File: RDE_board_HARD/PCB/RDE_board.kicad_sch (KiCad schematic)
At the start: 18 parts, among them J4 7772, J5 7772, J6 7772, J7 7772

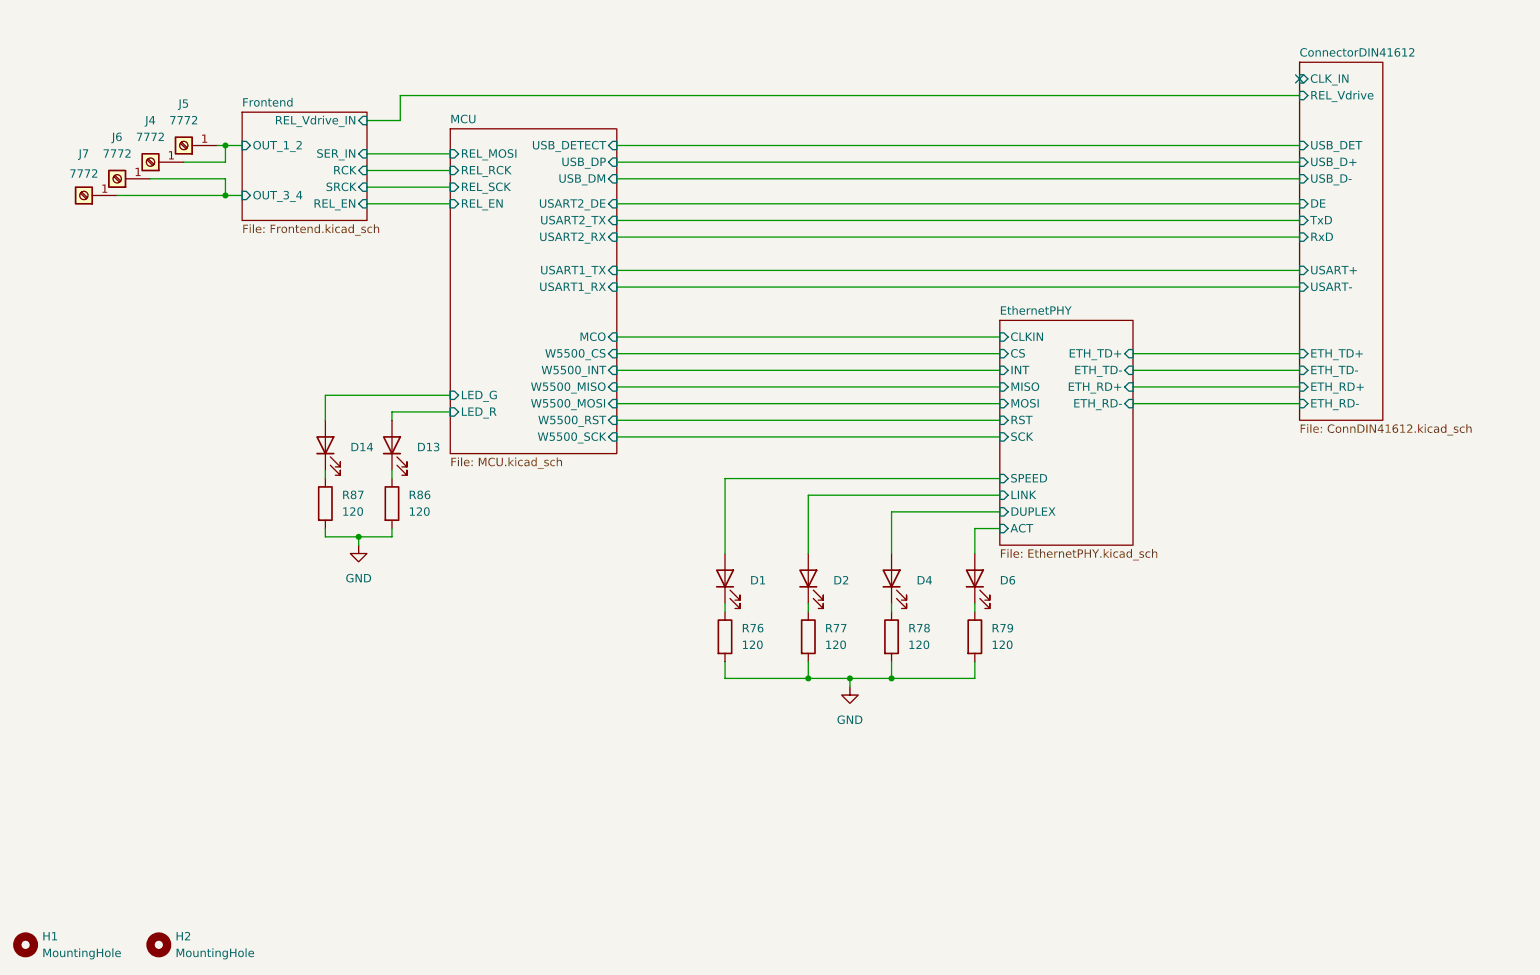
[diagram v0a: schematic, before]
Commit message: Added i2c for backplane config, testpoints. File organization
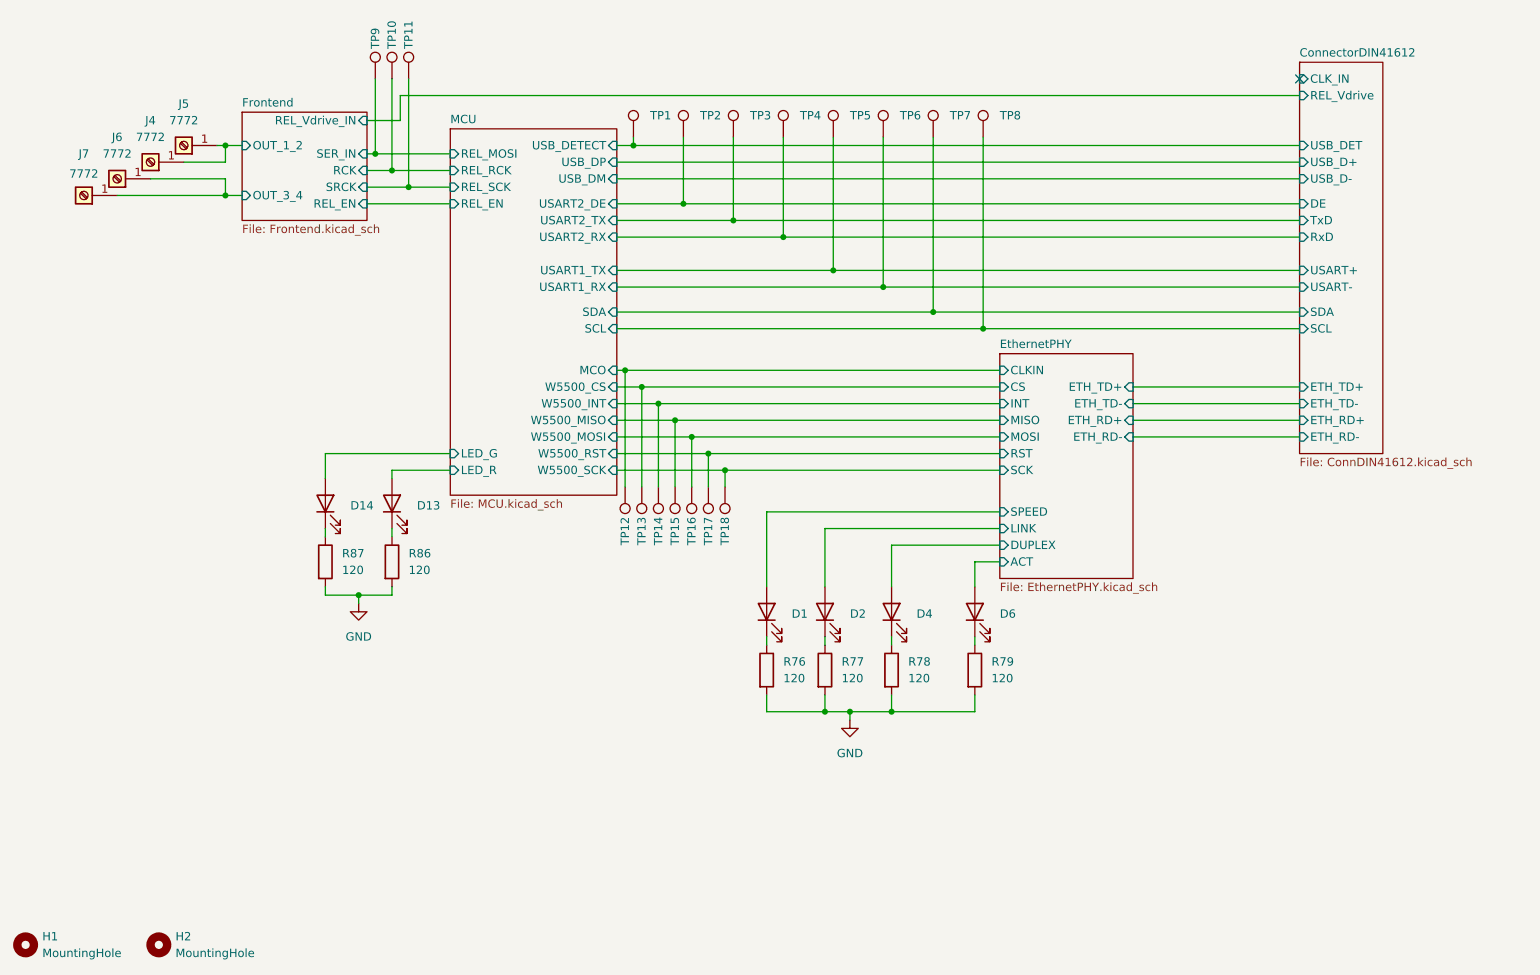
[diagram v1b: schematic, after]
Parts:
- added TP1, TP10, TP11, TP12, TP13, TP14, TP15, TP16, TP17, TP18, TP2, TP3, TP4, TP5, TP6, TP7, TP8, TP9: TestPoint, TestPoint:TestPoint_Pad_D1.0mm, symbol Connector:TestPoint
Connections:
- net ConnectorDIN41612/DE: now also TP2.1
- net ConnectorDIN41612/RxD: now also TP4.1
- net ConnectorDIN41612/TxD: now also TP3.1
- net ConnectorDIN41612/USART+: now also TP5.1
- net ConnectorDIN41612/USART-: now also TP6.1
- net ConnectorDIN41612/USB_DET: now also TP1.1
- net EthernetPHY/CLKIN: now also TP12.1
- net EthernetPHY/CS: now also TP13.1
- net EthernetPHY/INT: now also TP14.1
- net EthernetPHY/MISO: now also TP15.1
- net EthernetPHY/MOSI: now also TP16.1
- net EthernetPHY/RST: now also TP17.1
- net EthernetPHY/SCK: now also TP18.1
- net Frontend/RCK: now also TP10.1
- net Frontend/SER_IN: now also TP9.1
- net Frontend/SRCK: now also TP11.1
- new net ConnectorDIN41612/SCL: TP8.1
- new net ConnectorDIN41612/SDA: TP7.1
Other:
- sheet ConnectorDIN41612 ports: added SCL, SDA; removed none
- sheet MCU ports: added SCL, SDA; removed none
- moved on the sheet: D1, D13, D14, D2, D4, D6, R76, R77, R78, R79, R86, R87
